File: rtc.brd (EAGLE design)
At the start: 27.9 x 29.2 mm, 14 parts, among them U1 MCP79412, Y1 32.768 kHz

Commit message: v1.0
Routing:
- net VCC: track 46.6 -> 45.1 mm
- net SDA: track 30.1 -> 28.6 mm
- net SCL: track 32.1 -> 30.6 mm
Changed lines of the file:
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@@
 <layer number="209" name="209bmp" color="7" fill="1" visible="yes" active="yes"/>
 <layer number="210" name="210bmp" color="7" fill="1" visible="yes" active="yes"/>
+<layer number="211" name="211bmp" color="7" fill="1" visible="yes" active="yes"/>
+<layer number="212" name="212bmp" color="7" fill="1" visible="yes" active="yes"/>
+<layer number="213" name="213bmp" color="7" fill="1" visible="yes" active="yes"/>
+<layer number="214" name="214bmp" color="7" fill="1" visible="yes" active="yes"/>
+<layer number="215" name="215bmp" color="7" fill="1" visible="yes" active="yes"/>
+<layer number="216" name="216bmp" color="7" fill="1" visible="yes" active="yes"/>
 <layer number="250" name="Descript" color="7" fill="1" visible="no" active="no"/>
 <layer number="251" name="SMDround" color="7" fill="1" visible="no" active="no"/>
@@
 <contactref element="JP1" pad="2"/>
 <contactref element="C1" pad="1"/>
-<wire x1="20.32" y1="10.16" x2="20.32" y2="18.542" width="0.3048" layer="16"/>
 <via x="20.32" y="18.542" extent="1-16" drill="0.5"/>
 <wire x1="20.32" y1="18.542" x2="20.32" y2="21.336" width="0.3048" layer="1"/>
@@
 <wire x1="10.795" y1="18.923" x2="10.414" y2="18.542" width="0.3048" layer="1"/>
 <wire x1="10.795" y1="18.923" x2="11.176" y2="18.542" width="0.3048" layer="1"/>
-<wire x1="20.32" y1="10.16" x2="21.59" y2="8.89" width="0.3048" layer="16"/>
-<wire x1="21.59" y1="8.89" x2="25.273" y2="8.89" width="0.3048" layer="16"/>
+<wire x1="25.273" y1="8.89" x2="24.13" y2="8.89" width="0.3048" layer="16"/>
+<wire x1="24.13" y1="8.89" x2="20.32" y2="12.7" width="0.3048" layer="16"/>
+<wire x1="20.32" y1="12.7" x2="20.32" y2="18.542" width="0.3048" layer="16"/>
 </signal>
 <signal name="GND">
@@
 <wire x1="14.605" y1="24.384" x2="12.766" y2="24.384" width="0.3048" layer="1"/>
 <wire x1="12.766" y1="24.384" x2="12.7" y2="24.45" width="0.3048" layer="1"/>
-<wire x1="19.05" y1="8.89" x2="19.05" y2="21.717" width="0.3048" layer="16"/>
+<wire x1="19.05" y1="11.43" x2="19.05" y2="21.717" width="0.3048" layer="16"/>
 <wire x1="19.05" y1="21.717" x2="16.383" y2="24.384" width="0.3048" layer="16"/>
 <wire x1="16.383" y1="24.384" x2="14.605" y2="24.384" width="0.3048" layer="16"/>
@@
 <wire x1="12.766" y1="23.175" x2="13.335" y2="22.606" width="0.3048" layer="1"/>
 <wire x1="13.335" y1="22.606" x2="13.335" y2="20.3962" width="0.3048" layer="1"/>
-<wire x1="19.05" y1="8.89" x2="21.59" y2="6.35" width="0.3048" layer="16"/>
-<wire x1="21.59" y1="6.35" x2="25.527" y2="6.35" width="0.3048" layer="16"/>
+<wire x1="25.527" y1="6.35" x2="24.13" y2="6.35" width="0.3048" layer="16"/>
+<wire x1="24.13" y1="6.35" x2="19.05" y2="11.43" width="0.3048" layer="16"/>
 </signal>
 <signal name="SDA">
@@
 <contactref element="R3" pad="1"/>
 <contactref element="U1" pad="5"/>
-<wire x1="17.78" y1="7.62" x2="17.78" y2="20.32" width="0.3048" layer="16"/>
 <via x="17.78" y="20.32" extent="1-16" drill="0.5"/>
 <wire x1="16.51" y1="24.45" x2="16.51" y2="20.828" width="0.3048" layer="1"/>
@@
 <wire x1="16.51" y1="20.828" x2="16.129" y2="20.447" width="0.3048" layer="1"/>
 <wire x1="16.51" y1="20.828" x2="16.891" y2="20.447" width="0.3048" layer="1"/>
-<wire x1="17.78" y1="7.62" x2="21.59" y2="3.81" width="0.3048" layer="16"/>
-<wire x1="21.59" y1="3.81" x2="25.273" y2="3.81" width="0.3048" layer="16"/>
+<wire x1="25.273" y1="3.81" x2="24.13" y2="3.81" width="0.3048" layer="16"/>
+<wire x1="24.13" y1="3.81" x2="17.78" y2="10.16" width="0.3048" layer="16"/>
+<wire x1="17.78" y1="10.16" x2="17.78" y2="20.32" width="0.3048" layer="16"/>
 </signal>
 <signal name="BAT">
@@
 </signal>
 </signals>
-<errors>
-</errors>
 </board>
 </drawing>

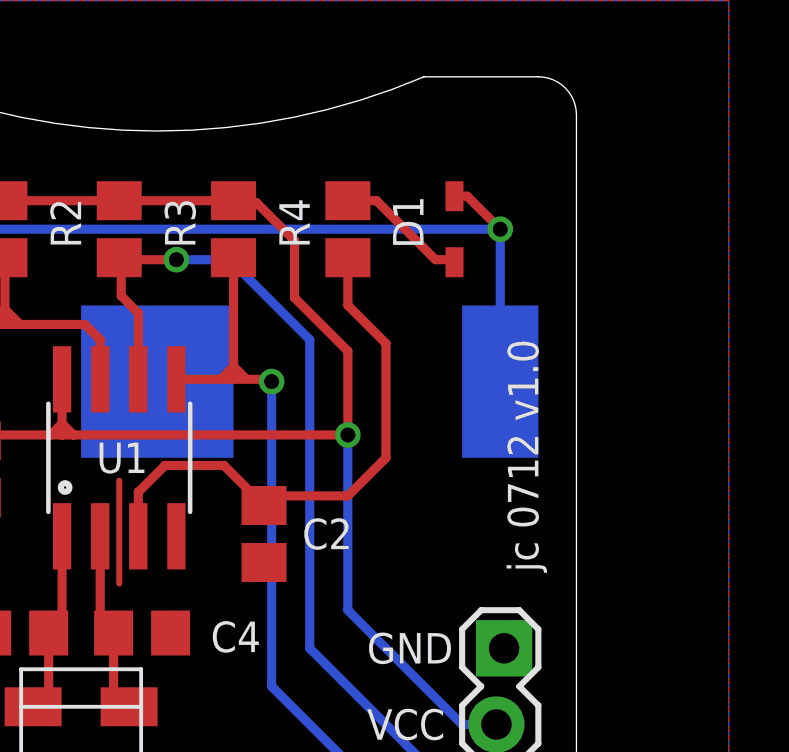
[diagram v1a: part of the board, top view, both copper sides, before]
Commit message: v1.1 Larger pads for D1.
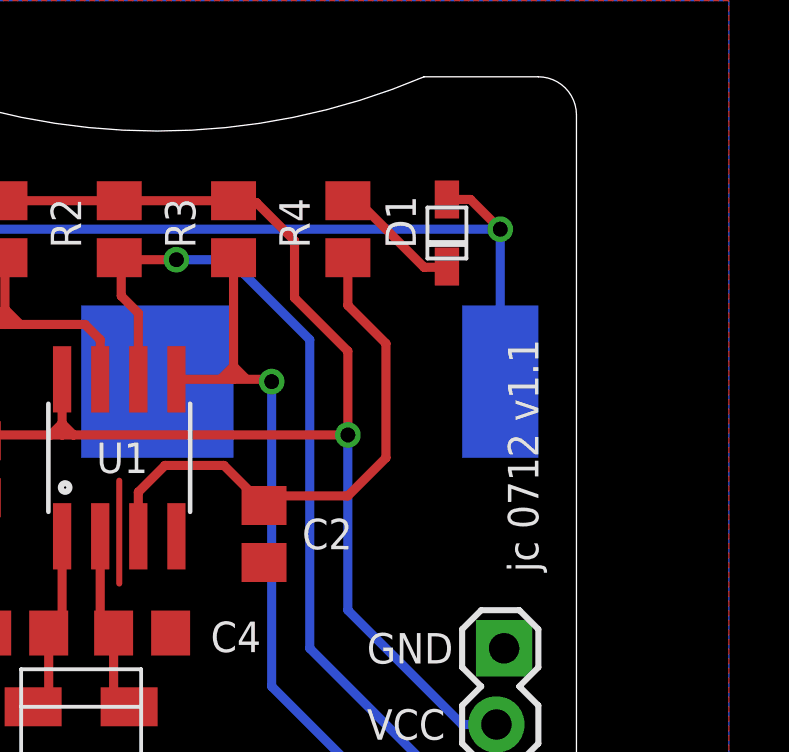
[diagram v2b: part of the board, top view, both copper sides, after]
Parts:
- D1: device zetex:SOD323 -> _jc:SOD-323F
- moved D1 0.28 mm to (23.6, 25.3), turned to 270 degrees
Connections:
- net BAT: now also D1.A; no longer D1.2
- net N$1: now also D1.K; no longer D1.1
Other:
- board text added: "jc 0712 v1.1"
- board text removed: "jc 0712 v1.0"
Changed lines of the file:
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@@
 <layer number="109" name="fp9" color="7" fill="1" visible="yes" active="yes"/>
 <layer number="110" name="fp0" color="7" fill="1" visible="yes" active="yes"/>
+<layer number="111" name="LPC17xx" color="7" fill="1" visible="yes" active="yes"/>
+<layer number="112" name="tSilk" color="7" fill="1" visible="yes" active="yes"/>
 <layer number="116" name="Patch_BOT" color="9" fill="4" visible="yes" active="yes"/>
 <layer number="121" name="_tsilk" color="7" fill="1" visible="yes" active="yes"/>
@@
 <layer number="123" name="tTestmark" color="7" fill="1" visible="yes" active="yes"/>
 <layer number="124" name="bTestmark" color="7" fill="1" visible="yes" active="yes"/>
+<layer number="125" name="_tNames" color="7" fill="1" visible="yes" active="yes"/>
+<layer number="126" name="_bNames" color="7" fill="1" visible="yes" active="yes"/>
+<layer number="127" name="_tValues" color="7" fill="1" visible="yes" active="yes"/>
+<layer number="128" name="_bValues" color="7" fill="1" visible="yes" active="yes"/>
 <layer number="131" name="tAdjust" color="7" fill="1" visible="yes" active="yes"/>
 <layer number="132" name="bAdjust" color="7" fill="1" visible="yes" active="yes"/>
 <layer number="144" name="Drill_legend" color="7" fill="1" visible="yes" active="yes"/>
 <layer number="151" name="HeatSink" color="7" fill="1" visible="yes" active="yes"/>
+<layer number="152" name="_bDocu" color="7" fill="1" visible="yes" active="yes"/>
 <layer number="199" name="Contour" color="7" fill="1" visible="yes" active="yes"/>
 <layer number="200" name="200bmp" color="1" fill="10" visible="no" active="no"/>
@@
 <layer number="215" name="215bmp" color="7" fill="1" visible="yes" active="yes"/>
 <layer number="216" name="216bmp" color="7" fill="1" visible="yes" active="yes"/>
+<layer number="217" name="217bmp" color="7" fill="1" visible="yes" active="yes"/>
+<layer number="218" name="218bmp" color="7" fill="1" visible="yes" active="yes"/>
+<layer number="219" name="219bmp" color="7" fill="1" visible="yes" active="yes"/>
+<layer number="220" name="220bmp" color="7" fill="1" visible="yes" active="yes"/>
+<layer number="221" name="221bmp" color="7" fill="1" visible="yes" active="yes"/>
+<layer number="222" name="222bmp" color="7" fill="1" visible="yes" active="yes"/>
+<layer number="223" name="223bmp" color="7" fill="1" visible="yes" active="yes"/>
+<layer number="224" name="224bmp" color="7" fill="1" visible="yes" active="yes"/>
+<layer number="248" name="Housing" color="7" fill="1" visible="yes" active="yes"/>
+<layer number="249" name="Edge" color="7" fill="1" visible="yes" active="yes"/>
 <layer number="250" name="Descript" color="7" fill="1" visible="no" active="no"/>
 <layer number="251" name="SMDround" color="7" fill="1" visible="no" active="no"/>
@@
 <text x="19.05" y="7.62" size="1.4224" layer="22" ratio="10" rot="MR0">MCP79412</text>
 <text x="22.86" y="5.715" size="1.4224" layer="22" ratio="10" rot="MR0">Real-Time Clock</text>
-<text x="21.59" y="3.81" size="1.4224" layer="22" ratio="10" rot="MR0">jc 0712 v1.0</text>
+<text x="21.59" y="3.81" size="1.4224" layer="22" ratio="10" rot="MR0">jc 0712 v1.1</text>
 <text x="19.05" y="1.905" size="1.4224" layer="22" ratio="10" rot="MR0">CC BY-SA</text>
 <text x="4.445" y="16.51" size="1.27" layer="21" ratio="10" rot="R90">CC BY-SA</text>
-<text x="26.67" y="13.97" size="1.016" layer="21" ratio="10" rot="R90">jc 0712 v1.0</text>
+<text x="26.67" y="13.97" size="1.016" layer="21" ratio="10" rot="R90">jc 0712 v1.1</text>
 </plain>
 <attributes>
@@
 <attribute name="VALUE" x="5.715" y="2.54" size="1.27" layer="27" rot="R90"/>
 </element>
-<element name="D1" library="zetex" package="SOD323" value="PMEG6002EJ" x="23.876" y="25.4" smashed="yes" rot="R90">
-<attribute name="OC_NEWARK" value="79R6078" x="23.876" y="25.4" size="1.778" layer="27" rot="R90" display="off"/>
-<attribute name="MPN" value="CDSOD323-T05C" x="23.876" y="25.4" size="1.778" layer="27" rot="R90" display="off"/>
-<attribute name="MF" value="" x="23.876" y="25.4" size="1.778" layer="27" rot="R90" display="off"/>
-<attribute name="OC_FARNELL" value="1824860" x="23.876" y="25.4" size="1.778" layer="27" rot="R90" display="off"/>
-<attribute name="NAME" x="22.842" y="24.754" size="1.016" layer="25" rot="R90"/>
-<attribute name="VALUE" x="25.681" y="24.5" size="1.016" layer="27" rot="R90"/>
+<element name="D1" library="_jc" package="SOD-323F" value="PMEG6002EJ" x="23.622" y="25.273" smashed="yes" rot="R270">
+<attribute name="NAME" x="22.588" y="24.754" size="1.016" layer="25" rot="R90"/>
+<attribute name="VALUE" x="21.817" y="26.173" size="1.016" layer="27" rot="R270"/>
 </element>
 <element name="B1" library="_jc" package="BAT-HLD-002-SMT" value="CR2016" x="13.97" y="20.32" smashed="yes" rot="MR180">
@@
 <signal name="BAT">
 <contactref element="JP2" pad="4"/>
-<contactref element="D1" pad="2"/>
+<contactref element="D1" pad="A"/>
 <contactref element="B1" pad="POS2"/>
 <contactref element="B1" pad="POS1"/>
@@
 <wire x1="3.81" y1="25.4" x2="25.4" y2="25.4" width="0.3048" layer="16"/>
 <wire x1="25.4" y1="25.4" x2="25.4" y2="20.32" width="0.3048" layer="16"/>
-<wire x1="23.876" y1="26.5" x2="24.3" y2="26.5" width="0.3048" layer="1"/>
-<wire x1="24.3" y1="26.5" x2="25.4" y2="25.4" width="0.3048" layer="1"/>
 <via x="25.4" y="25.4" extent="1-16" drill="0.5"/>
 <wire x1="2.667" y1="11.43" x2="2.667" y2="20.193" width="0.3048" layer="16"/>
 <wire x1="2.667" y1="20.193" x2="2.54" y2="20.32" width="0.3048" layer="16"/>
+<wire x1="23.622" y1="26.3906" x2="24.4094" y2="26.3906" width="0.3048" layer="1"/>
+<wire x1="24.4094" y1="26.3906" x2="25.4" y2="25.4" width="0.3048" layer="1"/>
 </signal>
 <signal name="N$1">
 <contactref element="R4" pad="2"/>
-<contactref element="D1" pad="1"/>
-<wire x1="20.32" y1="26.35" x2="21.275" y2="26.35" width="0.3048" layer="1"/>
-<wire x1="21.275" y1="26.35" x2="23.241" y2="24.384" width="0.3048" layer="1"/>
-<wire x1="23.241" y1="24.384" x2="23.792" y2="24.384" width="0.3048" layer="1"/>
-<wire x1="23.792" y1="24.384" x2="23.876" y2="24.3" width="0.3048" layer="1"/>
+<contactref element="D1" pad="K"/>
+<wire x1="20.32" y1="26.35" x2="20.64" y2="26.35" width="0.3048" layer="1"/>
+<wire x1="20.64" y1="26.35" x2="22.86" y2="24.13" width="0.3048" layer="1"/>
+<wire x1="22.86" y1="24.13" x2="23.5966" y2="24.13" width="0.3048" layer="1"/>
+<wire x1="23.5966" y1="24.13" x2="23.622" y2="24.1554" width="0.3048" layer="1"/>
 </signal>
 </signals>
+<errors>
+</errors>
 </board>
 </drawing>
